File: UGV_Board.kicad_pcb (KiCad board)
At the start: 2 copper layers, 19 parts, among them J1 I2C_EXPANSION, J2 Debug Header, J3 ESP_Header, SW1 SW_MCU_EN, SW2 SW_PICO_RST, SW3 SW_ESP_RST, U1 SC0915, U2 SPX1117M3-L-3-3

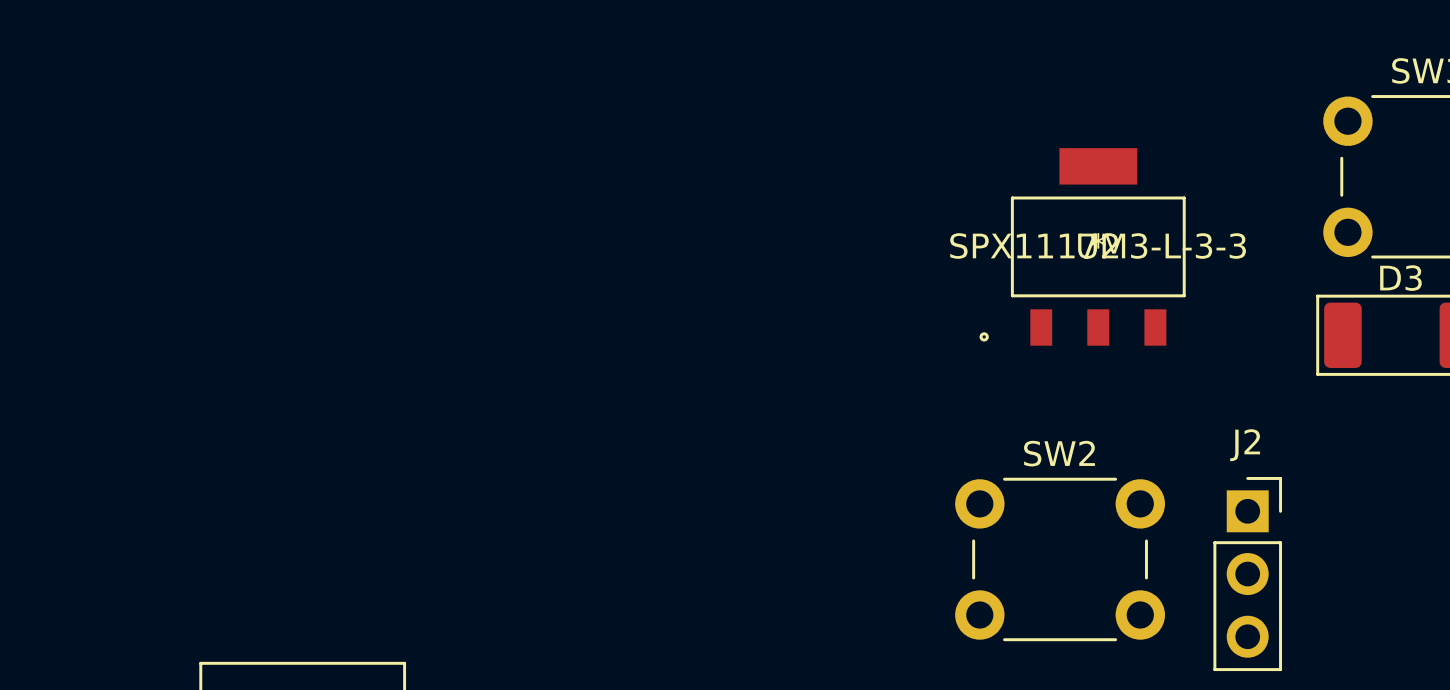
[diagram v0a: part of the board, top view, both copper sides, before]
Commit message: Buck + H-Bridge
Added
-Buck Convertor
-H-Bridge
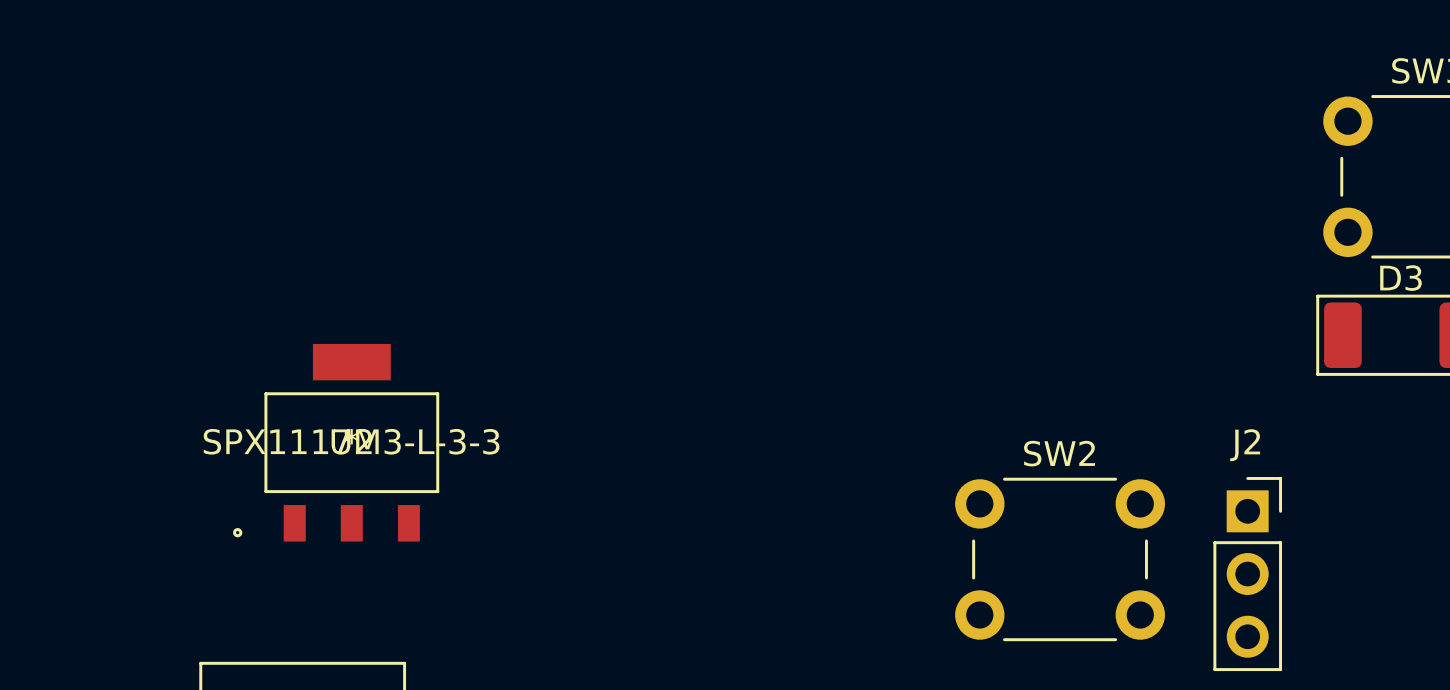
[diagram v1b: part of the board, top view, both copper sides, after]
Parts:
- moved U2 31.3 mm to (104.1, 88.9)
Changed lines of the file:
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@@
   )
   (footprint "Regulators:SPX1117M3-L-3-3&slash_TR" (layer "F.Cu")
-    (at 134.3738 80.9709)
+    (at 104.14 88.9)
     (property "Sheetfile" "UGV_Board.kicad_sch")
     (property "Sheetname" "")

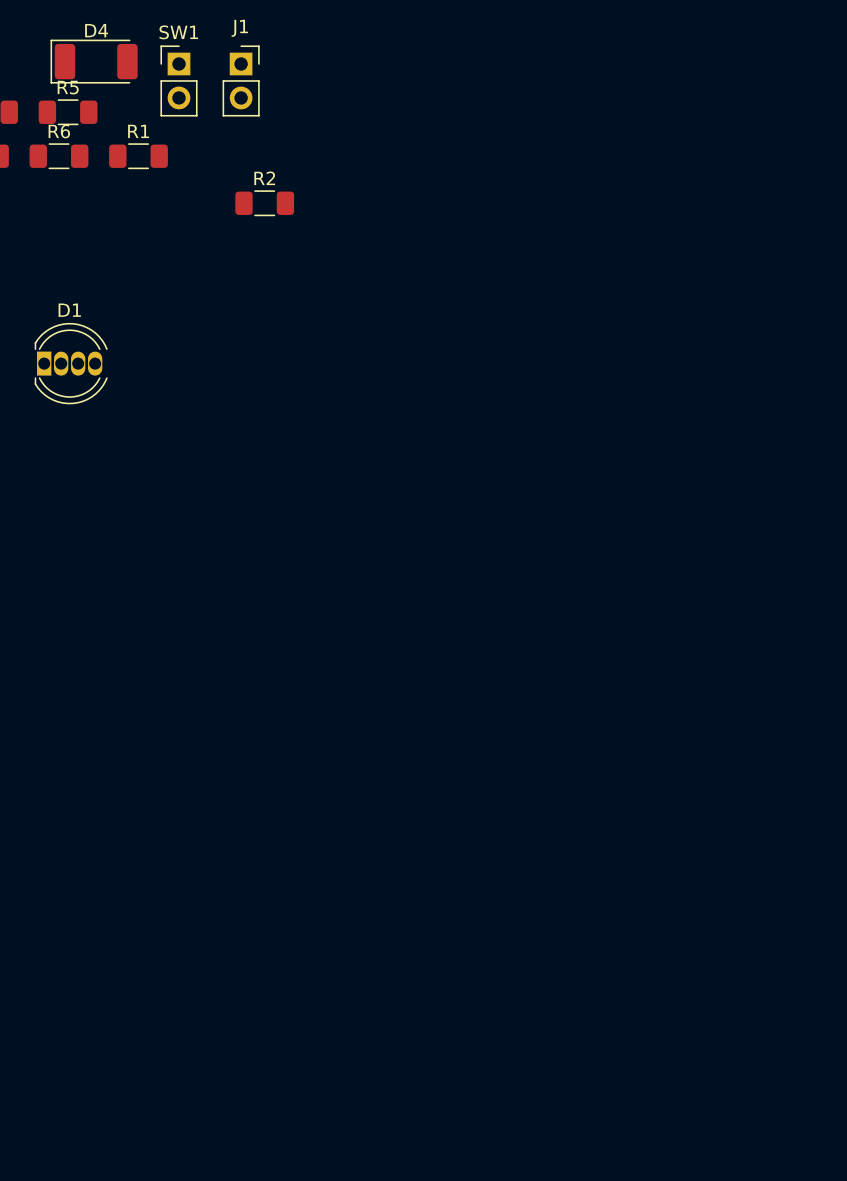
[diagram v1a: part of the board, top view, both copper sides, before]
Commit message: fixed i2c header footprint
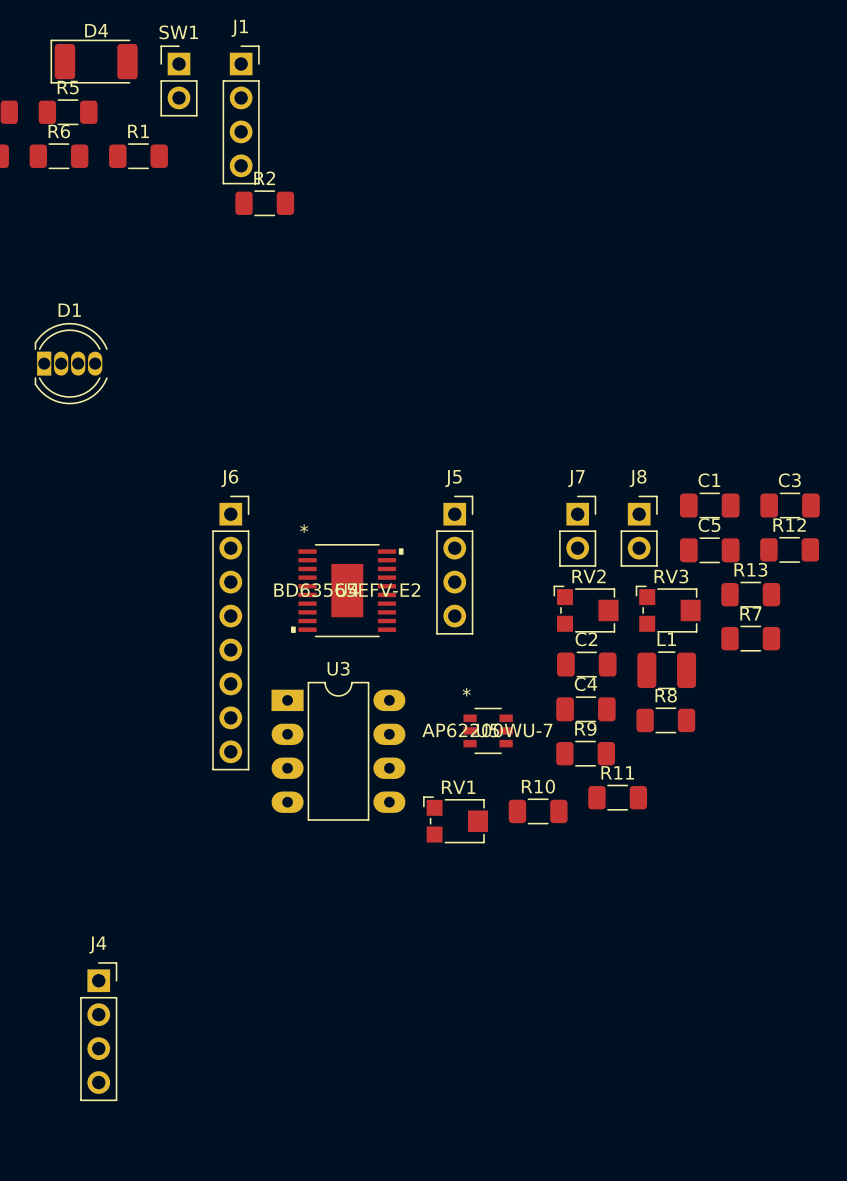
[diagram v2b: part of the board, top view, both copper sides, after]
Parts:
- added C1: 10uF, Capacitor_SMD:C_1206_3216Metric_Pad1.33x1.80mm_HandSolder, F.Cu at (215.9, 109.2)
- added C2: 22uF, Capacitor_SMD:C_1206_3216Metric_Pad1.33x1.80mm_HandSolder, F.Cu at (206.7, 121.1)
- added C3: 100nF, Capacitor_SMD:C_1206_3216Metric_Pad1.33x1.80mm_HandSolder, F.Cu at (221.9, 109.2)
- added C4: 1uF, Capacitor_SMD:C_1206_3216Metric_Pad1.33x1.80mm_HandSolder, F.Cu at (206.6, 124.5)
- added C5: 22 uF, Capacitor_SMD:C_1206_3216Metric_Pad1.33x1.80mm_HandSolder, F.Cu at (215.9, 112.6)
- added J4: RFLCTR_Header, Connector_PinSocket_2.54mm:PinSocket_1x04_P2.54mm_Vertical, F.Cu at (170.2, 144.8)
- added J5: RFLCTL_Header, Connector_PinSocket_2.54mm:PinSocket_1x04_P2.54mm_Vertical, F.Cu at (196.8, 109.9)
- added J6: IMU_Daughter_Header, Connector_PinSocket_2.54mm:PinSocket_1x08_P2.54mm_Vertical, F.Cu at (180.1, 109.9)
- added J7: Conn_01x02_Female, Connector_PinSocket_2.54mm:PinSocket_1x02_P2.54mm_Vertical, F.Cu at (206.0, 109.9)
- added J8: Conn_01x02_Female, Connector_PinSocket_2.54mm:PinSocket_1x02_P2.54mm_Vertical, F.Cu at (210.6, 109.9)
- added L1: 4.7uH, Inductor_SMD:L_1210_3225Metric_Pad1.42x2.65mm_HandSolder, F.Cu at (212.7, 121.5)
- added R10: 220, Resistor_SMD:R_1206_3216Metric_Pad1.30x1.75mm_HandSolder, F.Cu at (203.1, 132.1)
- added R11: 10k, Resistor_SMD:R_1206_3216Metric_Pad1.30x1.75mm_HandSolder, F.Cu at (209.0, 131.1)
- added R12: 10k, Resistor_SMD:R_1206_3216Metric_Pad1.30x1.75mm_HandSolder, F.Cu at (221.9, 112.5)
- added R13: 10k, Resistor_SMD:R_1206_3216Metric_Pad1.30x1.75mm_HandSolder, F.Cu at (219.0, 115.9)
- added R7: 220, Resistor_SMD:R_1206_3216Metric_Pad1.30x1.75mm_HandSolder, F.Cu at (219.0, 119.2)
- added R8: 220, Resistor_SMD:R_1206_3216Metric_Pad1.30x1.75mm_HandSolder, F.Cu at (212.6, 125.3)
- added R9: 220, Resistor_SMD:R_1206_3216Metric_Pad1.30x1.75mm_HandSolder, F.Cu at (206.6, 127.8)
- added RV1: R_Potentiometer, Potentiometer_SMD:Potentiometer_Bourns_TC33X_Vertical, F.Cu at (197.1, 132.8)
- added RV2: R_Potentiometer, Potentiometer_SMD:Potentiometer_Bourns_TC33X_Vertical, F.Cu at (206.9, 117.1)
- added RV3: R_Potentiometer, Potentiometer_SMD:Potentiometer_Bourns_TC33X_Vertical, F.Cu at (213.0, 117.1)
- added U3: LM393, Package_DIP:DIP-8_W7.62mm_LongPads, F.Cu at (184.3, 123.8)
- added U4: BD63565EFV-E2, Drivers_3rdParty:BD63565EFV-E2, F.Cu at (188.8, 115.6)
- added U5: AP62200WU-7, SMPS_3rdParty:AP62200WU-7, F.Cu at (199.3, 126.1)
- J1: footprint Connector_PinSocket_2.54mm:PinSocket_1x02_P2.54mm_Vertical -> Connector_PinSocket_2.54mm:PinSocket_1x04_P2.54mm_Vertical
- R1, R2, R3, R4, R5, R6: value 220 -> 330
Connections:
- D1 pad 2: Net-(R1-Pad1) -> Net-(D1-Pad2)
- J1 pad 1: SCL -> ESP_GND
- J1 pad 2: SDA -> SCL
- R1 pad 1: Net-(R1-Pad1) -> Net-(D1-Pad2)
- U1 pad 10: unconnected-(U1-Pad10) -> MAG_INT
- U1 pad 11: unconnected-(U1-Pad11) -> IMU_INT1
- U1 pad 12: unconnected-(U1-Pad12) -> IMU_INT2
- U1 pad 19: unconnected-(U1-Pad19) -> ENCL_SIG
- U1 pad 20: unconnected-(U1-Pad20) -> ENCR_SIG
- U1 pad 9: unconnected-(U1-Pad9) -> MAG_DRDY
